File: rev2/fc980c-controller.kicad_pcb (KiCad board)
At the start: 2 copper layers, 82.2 x 35.5 mm, 36 parts, among them J1 SWD, J2 USB, J3 KEYBOARD, SW1 BOOT0, U1 XC6206P332MR, U2 STM32F401CBUx, U3 USBLC6-2SC6, U4 M24C64-RMN6TP, U5 PCA9306DC, Y1 8MHz Cl 20pF

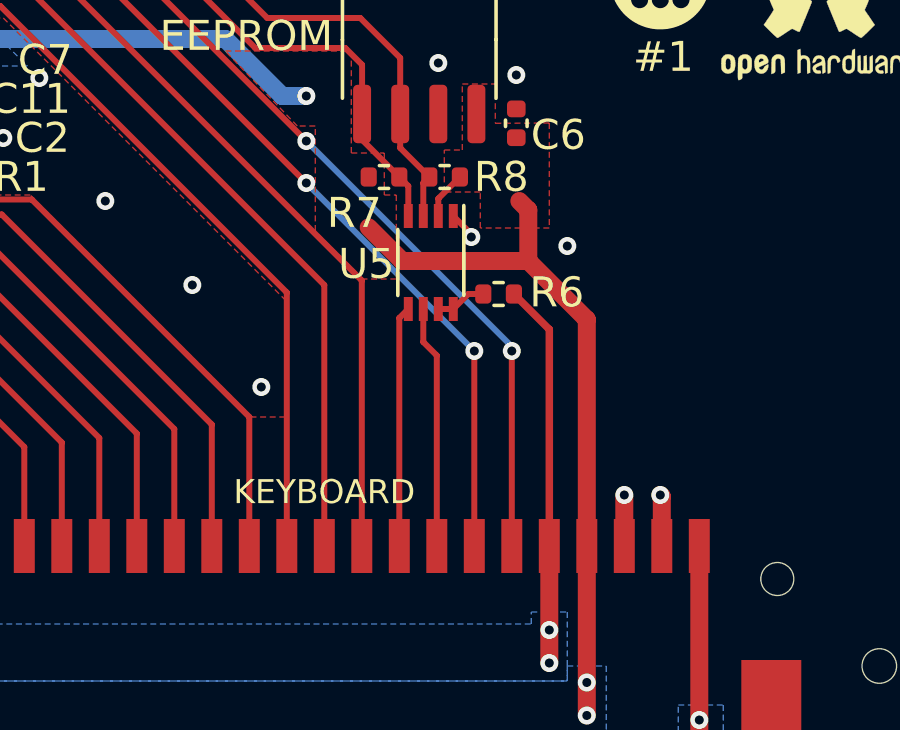
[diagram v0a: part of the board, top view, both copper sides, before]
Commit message: rev2: Add 5V pull-up to KEY_STATE pin
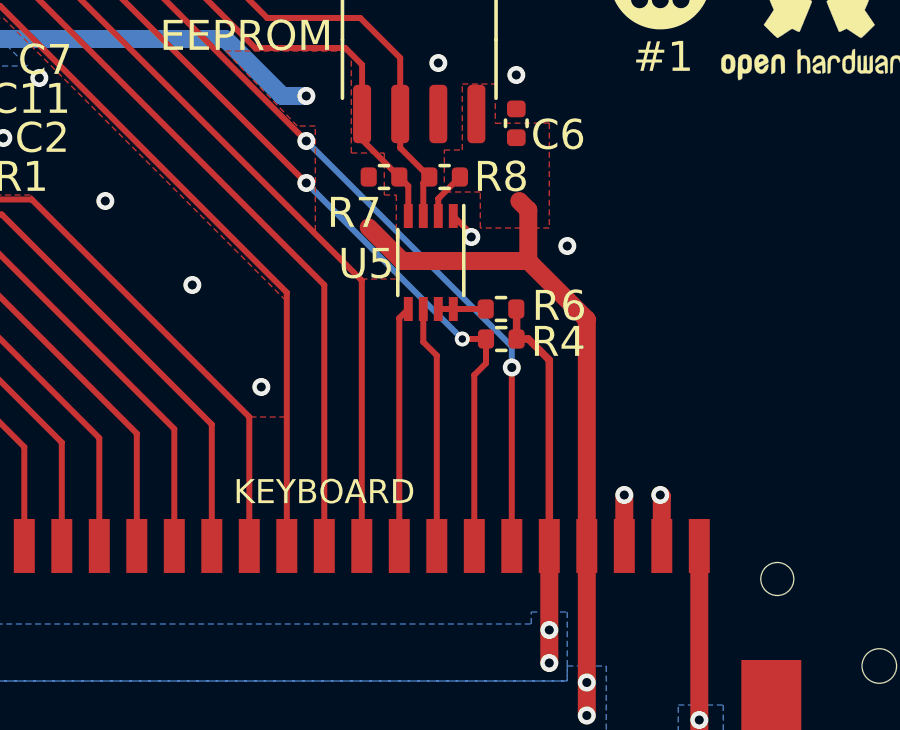
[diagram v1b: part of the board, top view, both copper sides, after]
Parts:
- added R4: 10k, Resistor_SMD:R_0402_1005Metric, F.Cu at (142.0, 56.3)
- moved R6 0.51 mm to (142.0, 55.3)
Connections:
- J3 pad 21: GND -> (no net)
- J3 pad 22: GND -> (no net)
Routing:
- net KEY_STATE: track 38.9 -> 39.7 mm
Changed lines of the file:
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@@
   )
   (footprint "Resistor_SMD:R_0402_1005Metric" (layer "F.Cu")
-    (at 141.91 54.8 180)
+    (at 141.99 55.3 180)
     (descr "Resistor SMD 0402 (1005 Metric), square (rectangular) end terminal, IPC_7351 nominal, (Body size source: IPC-SM-782 page 72, https://www.pcb-3d.com/wordpress/wp-content/uploads/ipc-sm-782a_amendment_1_and_2.pdf), generated with kicad-footprint-generator")
     (tags "resistor")
@@
     (property "Sheetname" "")
     (attr smd)
-    (fp_text reference "R6" (at -1.94 0.05) (layer "F.SilkS")
+    (fp_text reference "R6" (at -1.94 0.1) (layer "F.SilkS")
       (effects (font (size 1 1) (thickness 0.15)))
     )
@@
     (pad "20" smd rect (at -12.5 3.5 180) (size 0.7 1.8) (layers "F.Cu" "F.Paste" "F.Mask")
       (net 11 "FG") (pinfunction "Pin_20") (pintype "passive"))
-    (pad "21" smd rect (at -14.9 -1.6 180) (size 2 2.6) (layers "F.Cu" "F.Paste" "F.Mask")
-      (net 1 "GND"))
-    (pad "22" smd rect (at 13.65 -1.6 180) (size 2 2.6) (layers "F.Cu" "F.Paste" "F.Mask")
-      (net 1 "GND"))
+    (pad "21" smd rect (at -14.9 -1.6 180) (size 2 2.6) (layers "F.Cu" "F.Paste" "F.Mask"))
+    (pad "22" smd rect (at 13.65 -1.6 180) (size 2 2.6) (layers "F.Cu" "F.Paste" "F.Mask"))
   )
   (footprint "additional:logo" (layer "F.Cu")
@@
     )
   )
+  (footprint "Resistor_SMD:R_0402_1005Metric" (layer "F.Cu")
+    (at 142 56.3 180)
+    (descr "Resistor SMD 0402 (1005 Metric), square (rectangular) end terminal, IPC_7351 nominal, (Body size source: IPC-SM-782 page 72, https://www.pcb-3d.com/wordpress/wp-content/uploads/ipc-sm-782a_amendment_1_and_2.pdf), generated with kicad-footprint-generator")
+    (tags "resistor")
+    (property "Sheetfile" "fc980c-controller.kicad_sch")
+    (property "Sheetname" "")
+    (attr smd)
+    (fp_text reference "R4" (at -1.9 -0.1) (layer "F.SilkS")
+      (effects (font (size 1 1) (thickness 0.15)))
+    )
+    (fp_text value "10k" (at 0 1.17) (layer "F.Fab")
+      (effects (font (size 1 1) (thickness 0.15)))
+    )
+    (fp_text user "${REFERENCE}" (at 0 0) (layer "F.Fab")
+      (effects (font (size 0.26 0.26) (thickness 0.04)))
+    )
+    (fp_line (start -0.153641 0.38) (end 0.153641 0.38) (layer "F.SilkS") (width 0.12))
+    (fp_line (start -0.153641 -0.38) (end 0.153641 -0.38) (layer "F.SilkS") (width 0.12))
+    (fp_line (start 0.93 -0.47) (end 0.93 0.47) (layer "F.CrtYd") (width 0.05))
+    (fp_line (start 0.93 0.47) (end -0.93 0.47) (layer "F.CrtYd") (width 0.05))
+    (fp_line (start -0.93 0.47) (end -0.93 -0.47) (layer "F.CrtYd") (width 0.05))
+    (fp_line (start -0.93 -0.47) (end 0.93 -0.47) (layer "F.CrtYd") (width 0.05))
+    (fp_line (start -0.525 0.27) (end -0.525 -0.27) (layer "F.Fab") (width 0.1))
+    (fp_line (start -0.525 -0.27) (end 0.525 -0.27) (layer "F.Fab") (width 0.1))
+    (fp_line (start 0.525 -0.27) (end 0.525 0.27) (layer "F.Fab") (width 0.1))
+    (fp_line (start 0.525 0.27) (end -0.525 0.27) (layer "F.Fab") (width 0.1))
+    (pad "1" smd roundrect (at -0.51 0 180) (size 0.54 0.64) (layers "F.Cu" "F.Paste" "F.Mask") (roundrect_rratio 0.25)
+      (net 3 "+5V") (pintype "passive"))
+    (pad "2" smd roundrect (at 0.51 0 180) (size 0.54 0.64) (layers "F.Cu" "F.Paste" "F.Mask") (roundrect_rratio 0.25)
+      (net 13 "KEY_STATE") (pintype "passive"))
+    (model "${KICAD6_3DMODEL_DIR}/Resistor_SMD.3dshapes/R_0402_1005Metric.wrl"
+      (offset (xyz 0 0 0))
+      (scale (xyz 1 1 1))
+      (rotate (xyz 0 0 0))
+    )
+  )
   (footprint "Package_DFN_QFN:QFN-48-1EP_7x7mm_P0.5mm_EP5.6x5.6mm" (layer "F.Cu")
     (at 117.1 51.4 90)
@@
   (segment (start 117.375 47.358274) (end 115.333274 49.4) (width 0.25) (layer "B.Cu") (net 2))
   (segment (start 135.5 48.2) (end 134.7 48.2) (width 0.6) (layer "B.Cu") (net 2))
-  (segment (start 143.6 55.98) (end 142.42 54.8) (width 0.25) (layer "F.Cu") (net 3))
   (segment (start 92.6 57.6) (end 92.1 57.6) (width 0.2) (layer "F.Cu") (net 3))
   (segment (start 104.6 64.8) (end 111 64.8) (width 0.6) (layer "F.Cu") (net 3))
   (segment (start 88.55 53.75) (end 88.5 53.8) (width 0.6) (layer "F.Cu") (net 3))
+  (segment (start 143.6 57) (end 142.9 56.3) (width 0.25) (layer "F.Cu") (net 3))
   (segment (start 103.825 60.15) (end 103.825 62.675) (width 0.6) (layer "F.Cu") (net 3))
+  (segment (start 142.9 56.3) (end 142.51 56.3) (width 0.25) (layer "F.Cu") (net 3))
+  (segment (start 142.51 55.31) (end 142.5 55.3) (width 0.25) (layer "F.Cu") (net 3))
   (segment (start 111.9 65.7) (end 111.9 66.1) (width 0.6) (layer "F.Cu") (net 3))
   (segment (start 95.15 60.15) (end 103.825 60.15) (width 0.6) (layer "F.Cu") (net 3))
@@
   (segment (start 92.6 57.6) (end 95.15 60.15) (width 0.6) (layer "F.Cu") (net 3))
   (segment (start 143.6 63.2) (end 143.6 67.1) (width 0.6) (layer "F.Cu") (net 3))
+  (segment (start 142.51 56.3) (end 142.51 55.31) (width 0.25) (layer "F.Cu") (net 3))
+  (segment (start 143.6 63.2) (end 143.6 57) (width 0.25) (layer "F.Cu") (net 3))
   (segment (start 89.975 53.75) (end 88.55 53.75) (width 0.6) (layer "F.Cu") (net 3))
   (segment (start 111.9 66.1) (end 111.9 67.1) (width 0.6) (layer "F.Cu") (net 3))
   (segment (start 103.8 64) (end 104.6 64.8) (width 0.6) (layer "F.Cu") (net 3))
-  (segment (start 143.6 63.2) (end 143.6 55.98) (width 0.25) (layer "F.Cu") (net 3))
   (via (at 91.1 56.6) (size 0.6) (drill 0.3) (layers "F.Cu" "B.Cu") (net 3))
   (via (at 111.9 66.1) (size 0.6) (drill 0.3) (layers "F.Cu" "B.Cu") (net 3))
@@
   (segment (start 127.8 42) (end 120.4 42) (width 0.2) (layer "F.Cu") (net 12))
   (segment (start 135.5 49.7) (end 127.8 42) (width 0.2) (layer "F.Cu") (net 12))
-  (segment (start 142.35 63.2) (end 142.35 56.7) (width 0.2) (layer "F.Cu") (net 12))
+  (segment (start 142.35 63.2) (end 142.35 57.25) (width 0.2) (layer "F.Cu") (net 12))
   (segment (start 120.4 42) (end 117.85 44.55) (width 0.2) (layer "F.Cu") (net 12))
   (segment (start 117.85 44.55) (end 117.85 47.9625) (width 0.2) (layer "F.Cu") (net 12))
   (via (at 135.5 49.7) (size 0.6) (drill 0.3) (layers "F.Cu" "B.Cu") (net 12))
-  (via (at 142.35 56.7) (size 0.6) (drill 0.3) (layers "F.Cu" "B.Cu") (net 12))
+  (via (at 142.35 57.25) (size 0.6) (drill 0.3) (layers "F.Cu" "B.Cu") (net 12))
   (segment (start 142.35 56.55) (end 135.5 49.7) (width 0.2) (layer "B.Cu") (net 12))
-  (segment (start 142.35 56.7) (end 142.35 56.55) (width 0.2) (layer "B.Cu") (net 12))
+  (segment (start 142.35 57.25) (end 142.35 56.55) (width 0.2) (layer "B.Cu") (net 12))
   (segment (start 118.35 44.95) (end 118.35 47.9625) (width 0.2) (layer "F.Cu") (net 13))
   (segment (start 135.5 51.1) (end 127.2 42.8) (width 0.2) (layer "F.Cu") (net 13))
-  (segment (start 141.1 56.7) (end 141.1 63.2) (width 0.2) (layer "F.Cu") (net 13))
+  (segment (start 141.1 57.5) (end 141.1 63.2) (width 0.2) (layer "F.Cu") (net 13))
   (segment (start 127.2 42.8) (end 120.5 42.8) (width 0.2) (layer "F.Cu") (net 13))
+  (segment (start 141.49 56.3) (end 140.7 56.3) (width 0.2) (layer "F.Cu") (net 13))
   (segment (start 120.5 42.8) (end 118.35 44.95) (width 0.2) (layer "F.Cu") (net 13))
-  (via (at 141.1 56.7) (size 0.6) (drill 0.3) (layers "F.Cu" "B.Cu") (net 13))
+  (segment (start 141.1 57.5) (end 141.49 57.11) (width 0.2) (layer "F.Cu") (net 13))
+  (segment (start 141.49 57.11) (end 141.49 56.3) (width 0.2) (layer "F.Cu") (net 13))
+  (via (at 140.7 56.3) (size 0.5) (drill 0.25) (layers "F.Cu" "B.Cu") (net 13))
   (via (at 135.5 51.1) (size 0.6) (drill 0.3) (layers "F.Cu" "B.Cu") (net 13))
-  (segment (start 135.5 51.1) (end 141.1 56.7) (width 0.2) (layer "B.Cu") (net 13))
+  (segment (start 140.7 56.3) (end 135.5 51.1) (width 0.2) (layer "B.Cu") (net 13))
   (segment (start 139.85 63.2) (end 139.85 56.85) (width 0.2) (layer "F.Cu") (net 14))
   (segment (start 139.85 56.85) (end 139.4 56.4) (width 0.2) (layer "F.Cu") (net 14))
@@
   (segment (start 117.8 47.534314) (end 114.934314 50.4) (width 0.2) (layer "B.Cu") (net 47))
   (segment (start 114.934314 50.4) (end 112.1 50.4) (width 0.2) (layer "B.Cu") (net 47))
-  (segment (start 140.9 54.8) (end 140.4 55.3) (width 0.2) (layer "F.Cu") (net 48))
-  (segment (start 141.4 54.8) (end 140.9 54.8) (width 0.2) (layer "F.Cu") (net 48))
   (segment (start 139.9 55.3) (end 140.4 55.3) (width 0.2) (layer "F.Cu") (net 48))
+  (segment (start 141.48 55.3) (end 140.4 55.3) (width 0.2) (layer "F.Cu") (net 48))
   (zone (net 2) (net_name "VDDA") (layer "F.Cu") (hatch edge 0.508)
     (priority 1)

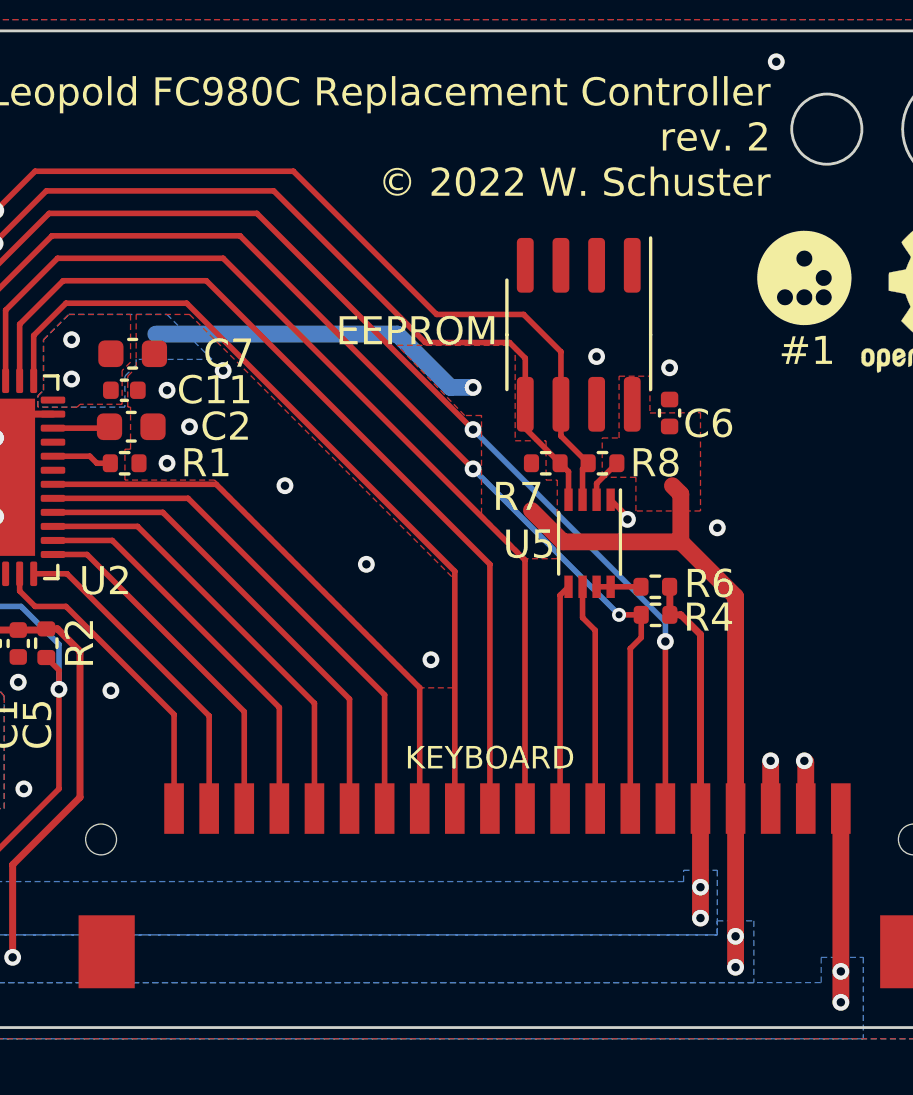
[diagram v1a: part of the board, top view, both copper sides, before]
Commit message: rev2: Drop I2C level shifter
Upon further review, using a 5V I2C bus should be unproblematic with a
5V tolerant MCU due to the open-drain design.
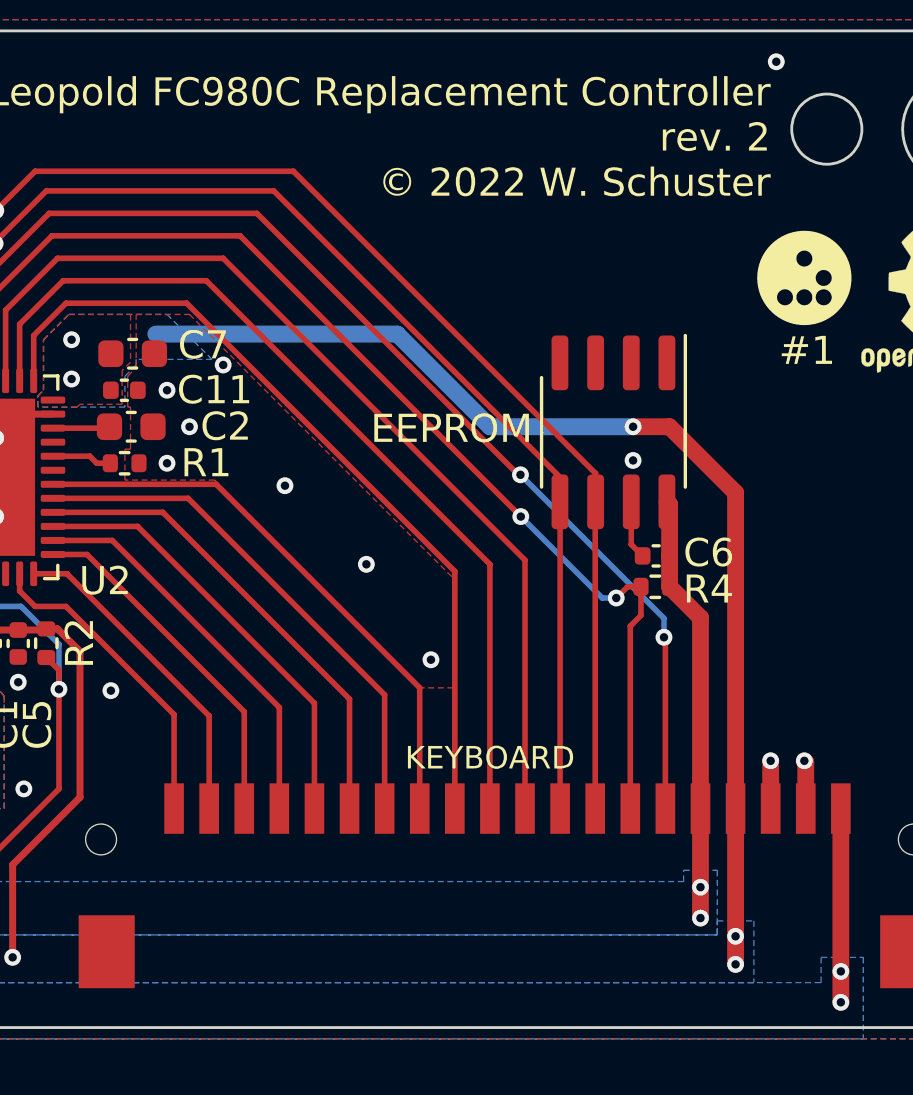
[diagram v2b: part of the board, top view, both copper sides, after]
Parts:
- removed R6: 200k, Resistor_SMD:R_0402_1005Metric
- removed R7, R8: 10k, Resistor_SMD:R_0402_1005Metric
- removed U5: PCA9306DC, Package_SO:VSSOP-8_2.3x2mm_P0.5mm
- moved C6 5.11 mm to (142.0, 54.2), turned to 180 degrees
- moved U4 3.69 mm to (140.5, 49.8)
- moved R4 1.00 mm to (142.0, 55.3)
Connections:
- C6 pad 1: VDDA -> +5V
- J3 pad 21: (no net) -> GND
- J3 pad 22: (no net) -> GND
- U2 pad 42: I2C_SCL_MCU -> I2C_SCL
- U2 pad 43: I2C_SDA_MCU -> I2C_SDA
- U4 pad 5: I2C_SDA_MCU -> I2C_SDA
- U4 pad 6: I2C_SCL_MCU -> I2C_SCL
- U4 pad 8: VDDA -> +5V
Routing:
- net I2C_SCL: track 8.09 -> 53.0 mm, vias 0 -> 2
- net I2C_SCL_MCU: track 43.8 -> 0.00 mm, vias 2 -> 0
- net I2C_SDA: track 8.02 -> 51.0 mm, vias 0 -> 2
- net I2C_SDA_MCU: track 41.9 -> 0.00 mm, vias 2 -> 0
- net +5V: track 47.2 -> 50.1 mm
- net VDDA: track 108.6 -> 110.8 mm
- net /VREF2_PCA9306: track 1.58 -> 0.00 mm
- net GND: track 24.5 -> 25.7 mm, vias 62 -> 59
- net KEY_STATE: track 39.7 -> 40.6 mm
